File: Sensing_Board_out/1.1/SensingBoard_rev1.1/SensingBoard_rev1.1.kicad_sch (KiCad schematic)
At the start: 52 parts, among them J1 USB_C_Receptacle, J3 F32R-1A7H1-11024, J4 GRPB052VWQP-RC, J5 HMTSW-102-X-X-S-X, J6 HMTSW-102-X-X-S-X, J7 3221-10-0300-00, J7 HMTSW-102-X-X-S-X, J8 HMTSW-102-X-X-S-X, SW1 PTS815 SJM 250 SMTR LFS, U1 ESP32C3, U2 BNO055, U3 MIC5504-3.3YM5, U4 FT232RQ

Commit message: finished power board
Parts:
- removed J5, J6, J7, J8: HMTSW-102-X-X-S-X, HMTSW-102-X-X-S-X:SAMTEC_HMTSW-102-X-X-S-X, symbol HMTSW-102-X-X-S-X:HMTSW-102-X-X-S-X
- added C10 (x4): 1uF, Capacitor_SMD:C_0201_0603Metric, symbol Device:C
- added C14 (x2): 18pF, Capacitor_SMD:C_0201_0603Metric, symbol Device:C
- added C17 (x2): 1.6pF, Capacitor_SMD:C_0402_1005Metric, symbol Device:C
- added C17: 100nF, Capacitor_SMD:C_0402_1005Metric, symbol Device:C
- added C9: 2.2uF, Capacitor_SMD:C_0402_1005Metric, symbol Device:C
- added C9 (x4): 10uF, Capacitor_SMD:C_0603_1608Metric, symbol Device:C
- added FB1: 120R-3A, Capacitor_SMD:C_0805_2012Metric, symbol Device:FerriteBead
- added J5, J6, J7, J9: RS1-02-G, CONN_RS1-02-G_ADM, symbol RS1-02-G:RS1-02-G
- added L1, L2: 2nH, Inductor_SMD:L_01005_0402Metric, symbol Device:L
- added R14 (x3), R15: 10k, Resistor_SMD:R_0201_0603Metric, symbol Device:R_US
- added SW2: PTS815 SJM 250 SMTR LFS, SW4_PTS815 SJM 250 SMTR LFS_CNK, symbol PTS815:PTS815_SJM_250_SMTR_LFS
- added U5: MIC5504-1.8YM5, Package_TO_SOT_SMD:SOT-23-5, symbol Regulator_Linear:MIC5504-1.8YM5
- added U6: MCP1700x-280xxTT, Package_TO_SOT_SMD:SOT-23, symbol Regulator_Linear:MCP1700x-280xxTT
- added Y1: ABM8G-40.000MHZ-18-D2Y-T, CRYSTAL_ABM8G_ABR, symbol ABM8G_40_000MHZ_18_D2Y_T:ABM8G-40.000MHZ-18-D2Y-T
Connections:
- net +3.3V: now also U1.17 (VDD3P3_CPU), U1.31 (VDDA), U1.32 (VDDA), L2.1, R14.1, R15.1; no longer U1.2 (VDD3P3), U1.3 (VDD3P3)
- net D9: now also SW2.1
- net DRV_FAULT: now also J7.1
- net DRV_SLEEP: now also J7.2
- net GND: now also ANT1.GND1, ANT1.GND2, C16.1, C17.2, J3.2, C10.2, C10.2, C10.2, C10.2, C14.2, C14.2, C17.2, C17.2, C17.2, C9.2, C9.2, C9.2, C9.2, C9.2, J9.1, SW2.4, U5.2 (GND), U6.1 (GND), Y1.2 (GND), Y1.4 (GND)
- net MOTOR1_AIN1: now also J5.2
- net MOTOR1_AIN2: now also J5.1
- net MOTOR2_BIN1: now also J6.2
- net MOTOR2_BIN2: now also J6.1
- net VDC: now also C10.1, C10.1, C9.1, C9.1, J9.2, U5.1 (VIN), U5.3 (EN), U6.3 (VI)
- net at ANT1.SIG: now also C17.1, L1.2
- net CHIP_EN: now reaches SW1.1
- net CHIP_EN: now also U1.7 (CHIP_EN)
- net at U1.1 (LNA_IN): now also C17.1, L1.1
- net VDD3P3_RTC: now reaches U1.11 (VDD3P3_RTC)
- net VDD_SPI: now reaches U1.18 (VDD_SPI)
- net SPIHD: now reaches U1.19 (SPIHD)
- net SPIWP: now reaches U1.20 (SPIWP)
- net SPICS0: now reaches U1.21 (SPICS0)
- net SPICLK: now reaches U1.22 (SPICLK)
- net SPID: now reaches U1.23 (SPID)
- net SPIQ: now reaches U1.24 (SPIQ)
- net at U1.29 (XTAL_N): now also C14.1, Y1.1
- net at U1.30 (XTAL_P): now also C14.1, Y1.3
- net IO40/CAM_SDA: now reaches J3.3
- net IO40/CAM_SDA: now also R14.2
- net at J3.4: now also FB1.2
- net IO39/CAM_SCL: now reaches J3.5
- net IO39/CAM_SCL: now also R14.2
- net CAM_RESET: now reaches J3.6
- net CAM_RESET: now also R14.2
- new net: C17.1, L2.2, U1.2 (VDD3P3), U1.3 (VDD3P3)
- new net: R15.2, SW2.2
- new net +1V8: C10.1, C9.1, U5.5 (VOUT)
- new net +2V8: C10.1, C9.1, C9.1, FB1.1, R14.1, R14.1, U6.2 (VO)
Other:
- note added: "1v8 LDO"
- note added: "2v8 LDO"
- note added: "B2B HEADERS (female)"
- note added: "BOOT"
- note added: "RESET"
- note removed: "B2B HEADERS"
- moved on the sheet: ANT1, C10, C14, C15, C16, C17, D5, D6, J3, J4, R11, R12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

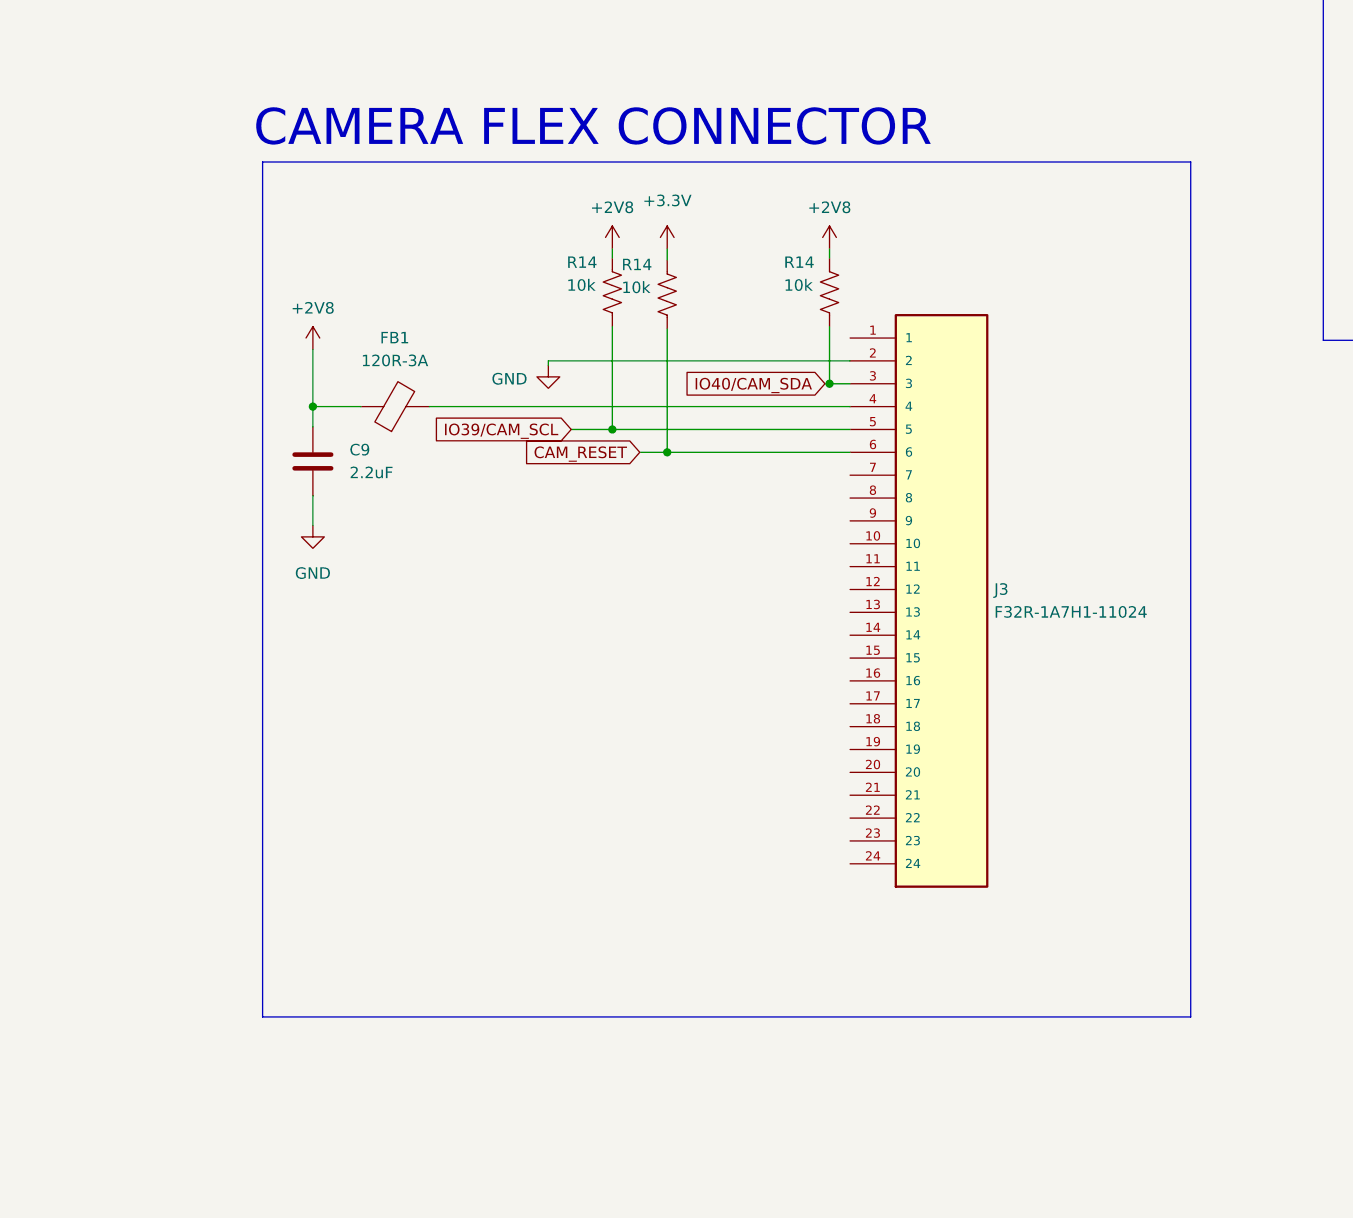
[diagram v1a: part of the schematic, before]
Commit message: fixing POE board symbols + circuit
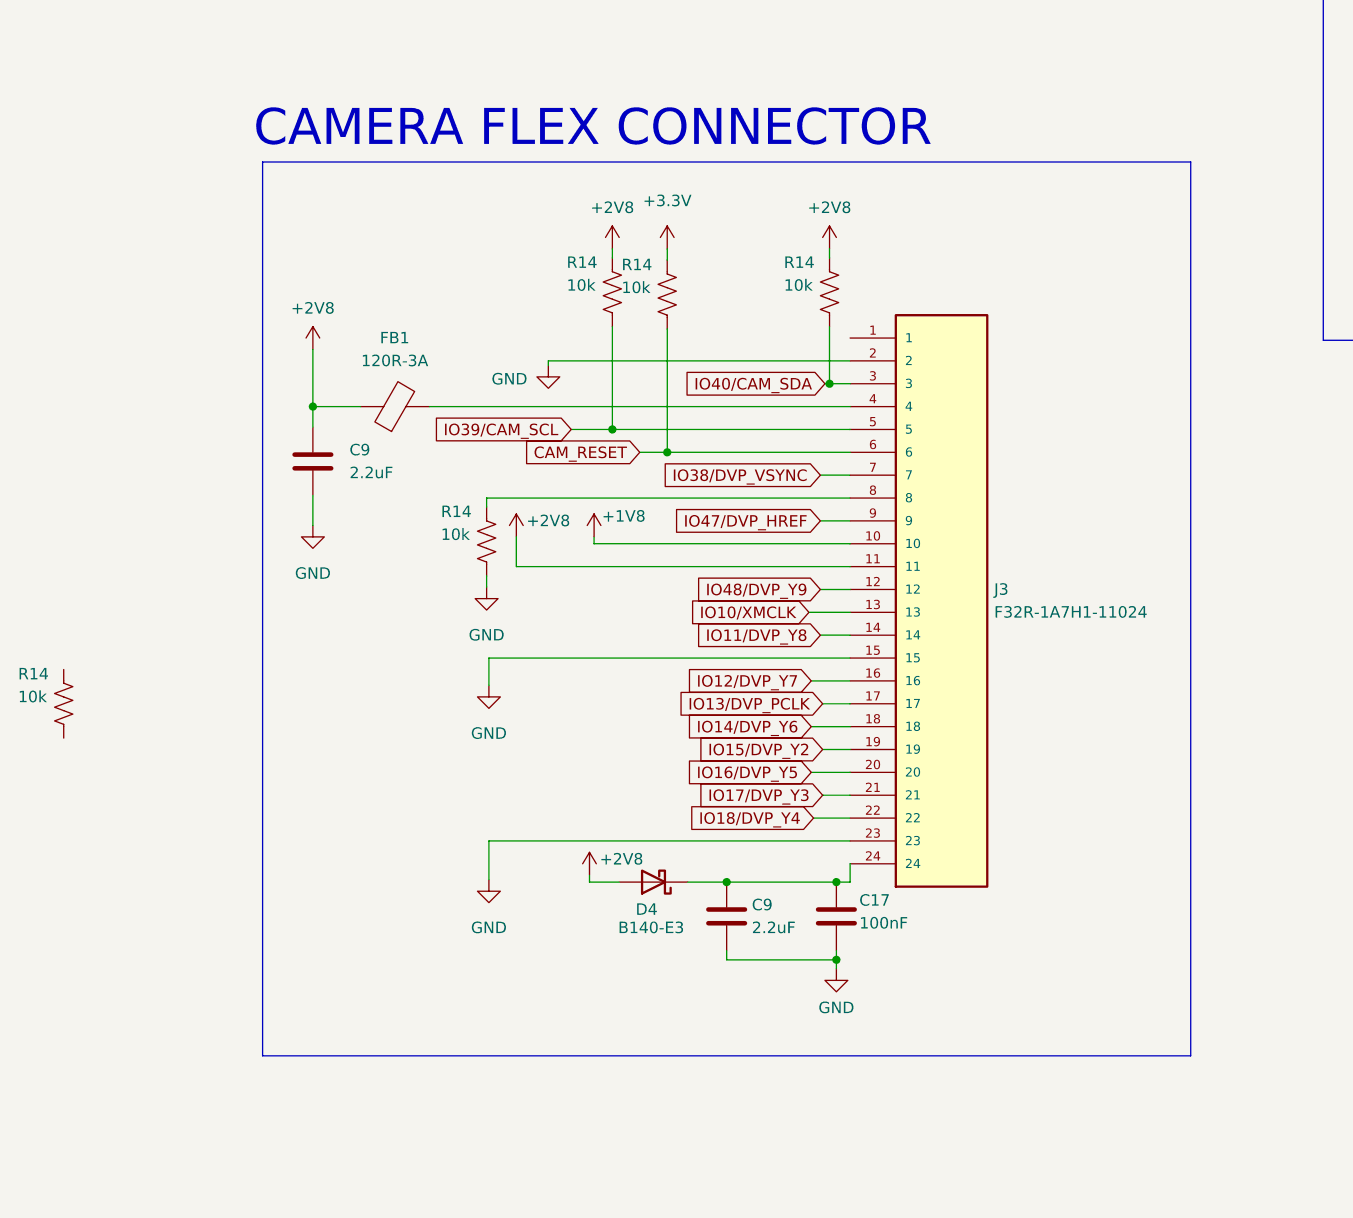
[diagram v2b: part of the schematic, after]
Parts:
- added C17: 100nF, Capacitor_SMD:C_0402_1005Metric, symbol Device:C
- added C9: 2.2uF, Capacitor_SMD:C_0402_1005Metric, symbol Device:C
- added D4: B140-E3, Diode_SMD:D_SMA, symbol Diode:B140-E3
- added R14 (x2): 10k, Resistor_SMD:R_0201_0603Metric, symbol Device:R_US
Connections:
- net +1V8: now also J3.10
- net +2V8: now also J3.11, D4.2 (A)
- net GND: now also J3.15, J3.23, C17.2, C9.2, R14.2
- net IO48/DVP_Y9: now reaches J3.12
- net IO10/XMCLK: now reaches J3.13
- net IO11/DVP_Y8: now reaches J3.14
- net IO12/DVP_Y7: now reaches J3.16
- net IO13/DVP_PCLK: now reaches J3.17
- net IO14/DVP_Y6: now reaches J3.18
- net IO15/DVP_Y2: now reaches J3.19
- net IO16/DVP_Y5: now reaches J3.20
- net IO17/DVP_Y3: now reaches J3.21
- net IO18/DVP_Y4: now reaches J3.22
- net at J3.24: now also C17.1, C9.1, D4.1 (K)
- net IO38/DVP_VSYNC: now reaches J3.7
- net at J3.8: now also R14.1
- net IO47/DVP_HREF: now reaches J3.9

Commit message: updates
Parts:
- removed R14: 10k, Resistor_SMD:R_0201_0603Metric, symbol Device:R_US
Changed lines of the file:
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@@
-    )
-  )
-  (symbol (lib_id "Device:R_US") (at 0 285.75 0) (unit 1)
-    (in_bom yes) (on_board yes) (dnp no)
-    (property "Reference" "R14" (at -5.08 282.448 0)
-      (effects (font (size 1.27 1.27)) (justify left))
-    )
-    (property "Value" "10k" (at -5.08 284.988 0)
-      (effects (font (size 1.27 1.27)) (justify left))
-    )
-    (property "Footprint" "Resistor_SMD:R_0201_0603Metric" (at 1.016 286.004 90)
-      (effects (font (size 1.27 1.27)) hide)
-    )
-    (property "Datasheet" "~" (at 0 285.75 0)
-      (effects (font (size 1.27 1.27)) hide)
-    )
-    (pin "1")
-    (pin "2")
-    (instances
-      (project "MachGen1B"
-        (path "/a8d93769-5183-4e19-8aae-3bec0e5cb94a"
-          (reference "R14") (unit 1)
-        )
-      )
-      (project "SensingBoard_rev1.1"
-        (path "/b61d80ec-963d-4516-bd15-8e7f6f5207da"
-          (reference "R26") (unit 1)
-        )
-      )
     )
   )

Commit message: updates
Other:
- note added: "Schematic Review: Swap with ESP32S3"
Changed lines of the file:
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@@
     (effects (font (size 4 4)) (justify left bottom))
+  )
+  (text "Schematic Review:\nSwap with ESP32S3" (at 607.314 143.256 0)
+    (effects (font (size 1.27 1.27)) (justify left bottom))
   )
   (text "HEADERS" (at 468.122 27.94 0)

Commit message: sense board
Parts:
- removed C14, C15: 22pF, Capacitor_SMD:C_0201_0603Metric, symbol Device:C
- removed C16: 10uF, Capacitor_SMD:C_0603_1608Metric, symbol Device:C
- removed C17: 100nF, Capacitor_SMD:C_0402_1005Metric, symbol Device:C
- removed C17: 1uF, Capacitor_SMD:C_0201_0603Metric, symbol Device:C
- removed J4: GRPB052VWQP-RC, GRPB052VWQP-RC:GRPB052VWQPRC, symbol GRPB052VWQP-RC:GRPB052VWQP-RC
- removed R14 (x3): 10k, Resistor_SMD:R_0201_0603Metric, symbol Device:R_US
- removed U1: ESP32C3, ESP32C3:QFN32_5X5MM, symbol ESP32C3:ESP32C3
- removed XTAL1: ABS07-32.768KHZ-7-T, XTAL_ABS07-32.768KHZ-7-T_ABR, symbol ABS07-32.768KHZ-7-T:ABS07-32.768KHZ-7-T
- added C17 (x7): 100nF, Capacitor_SMD:C_0402_1005Metric, symbol Device:C
- added C17: 10nF, Capacitor_SMD:C_0402_1005Metric, symbol Device:C
- added C17: 4.7uF, Capacitor_SMD:C_0402_1005Metric, symbol Device:C
- added C9 (x3): 2.2uF, Capacitor_SMD:C_0402_1005Metric, symbol Device:C
- added R11 (x2): 0k, Resistor_SMD:R_0201_0603Metric, symbol Device:R_US
- added R14: 10k, Resistor_SMD:R_0201_0603Metric, symbol Device:R_US
- added R14 (x2): 4.7k, Resistor_SMD:R_0201_0603Metric, symbol Device:R_US
- added R14: 499, Resistor_SMD:R_0201_0603Metric, symbol Device:R_US
- added U7: ESP32-S3, QFN56_7X7_EXP, symbol ESP32S3:ESP32-S3
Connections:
- net +2V8: now also R11.2
- net +3.3V: now also C17.1, C17.1, C17.1, C17.1, C17.1, C17.1, C17.1, C9.1, C9.1, C9.1, R11.2, R14.1, U7.20 (VDD3P3_RTC), U7.46 (VDD3P3_CPU), U7.55 (VDDA), U7.56 (VDDA)
- net CAM_RESET: now also C17.1, R14.2
- net CHIP_EN: now also U7.4 (CHIP_PU)
- net GND: now also C17.2, C17.2, C17.2, C17.2, C17.2, C17.2, C17.2, C17.2, C17.2, C9.2, C9.2, C9.2, U7.57 (GND)
- net IO10/XMCLK: now also U7.15 (GPIO10)
- net IO11/DVP_Y8: now also U7.16 (GPIO11)
- net IO12/DVP_Y7: now also U7.17 (GPIO12)
- net IO13/DVP_PCLK: now also U7.18 (GPIO13)
- net IO14/DVP_Y6: now also U7.19 (GPIO14)
- net IO15/DVP_Y2: now also U7.21 (XTAL_32K_P)
- net IO16/DVP_Y5: now also U7.22 (XTAL_32K_N)
- net IO17/DVP_Y3: now also U7.23 (GPIO17)
- net IO18/DVP_Y4: now also U7.24 (GPIO18)
- net IO38/DVP_VSYNC: now also U7.43 (GPIO38)
- net IO47/DVP_HREF: now also U7.37 (SPICLK_P)
- net IO48/DVP_Y9: now also U7.36 (SPICLK_N)
- net RX_D7: now also U7.50 (U0RXD)
- net SPICLK: now also U7.33 (SPICLK)
- net SPICS0: now also U7.32 (SPICS0)
- net SPID: now also U7.35 (SPID)
- net SPIHD: now also U7.30 (SPIHD)
- net SPIQ: now also U7.34 (SPIQ)
- net SPIWP: now also U7.31 (SPIWP)
- net TX_D6: now also R14.2
- net USB_DN: now also U7.25 (GPIO19)
- net USB_DP: now also U7.26 (GPIO20)
- net VDD_SPI: now also U7.29 (VDD_SPI)
- net at C14.1, Y1.1: now also U7.53 (XTAL_N)
- net at C14.1, Y1.3: now also U7.54 (XTAL_P)
- net at L2.2: now also C17.1, U7.2 (VDD3P3), U7.3 (VDD3P3)
- net at C17.1, L1.1: now also U7.1 (LNA_IN)
- net IO39/CAM_SCL renamed MTCK/IO39/CAM_SCL
- net MTCK/IO39/CAM_SCL: now also R14.2, U7.44 (MTCK)
- net IO40/CAM_SDA renamed MTDO/IO40/CAM_SDA
- net MTDO/IO40/CAM_SDA: now also R14.2, U7.45 (MTDO)
- new net: R11.1, R11.1, R14.1, R14.1
- new net: R14.1, U7.49 (U0TXD)
- new net D0/A0: U7.6 (GPIO1)
- new net D10/A10/MOSI: U7.14 (GPIO9)
- new net D1/A1: U7.7 (GPIO2)
- new net D2/A2: U7.8 (GPIO3)
- new net D3/A3: U7.9 (GPIO4)
- new net D4/I2C_SDA: U7.10 (GPIO5)
- new net D5/I2C_SCL: U7.11 (GPIO6)
- new net D8/A8/SCK: U7.12 (GPIO7)
- new net D9/A9/MISO: U7.13 (GPIO8)
- new net GPIO0: U7.5 (GPIO0)
- new net IO21/USER_LED: U7.27 (GPIO21)
- new net MTDI/IO41/PDM_DATA: U7.47 (MTDI)
- new net MTMS/IO42/PDM_CLK: U7.48 (MTMS)
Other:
- note removed: "HEADERS"
- note removed: "Schematic Review: Swap with ESP32S3"
- moved on the sheet: ANT1, C14, C17, J3, L1, Y1

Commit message: completed sense board
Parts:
- removed D5: LED, LED_SMD:LED_0603_1608Metric, symbol Device:LED
- removed R17: 100, Resistor_SMD:R_0201_0603Metric, symbol Device:R_US
- added C17: 100nF, Capacitor_SMD:C_0402_1005Metric, symbol Device:C
- added U8: GD25D05CT, Package_SO:SOP-8_3.9x4.9mm_P1.27mm, symbol Memory_Flash:GD25D05CT
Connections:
- net D9 is gone; now on net GPIO0: SW2.1
- net +3.3V: now also R16.2, C17.1, U8.8 (VCC)
- net D0/A0: now also R12.2
- net D1/A1: now also R12.2
- net D2/A2: now also R12.2
- net D3/A3: now also R12.2
- net GND: now also C17.2, U8.4 (VSS)
- net IO21/USER_LED: now also D6.1 (K)
- net SPICLK: now also U8.6 (SCLK)
- net SPICS0: now also U8.1 (~{CS})
- net SPID: now also U8.5 (SI/IO0)
- net SPIQ: now also U8.2 (O1/SO)
- net SPIWP: now also U8.3 (~{WP})
- net GPIO34: now reaches R11.2
- net GPIO34: now also U7.39 (GPIO34)
- net at R16.1: now also D6.2 (A)
- net GPIO33: now reaches R11.2
- net GPIO33: now also U7.38 (GPIO33)
- net GPIO37: now reaches R11.2
- net GPIO37: now also U7.42 (GPIO37)
- net GPIO35: now reaches R11.2
- net GPIO35: now also U7.40 (GPIO35)
- net GPIO36: now reaches R11.2
- net GPIO36: now also U7.41 (GPIO36)

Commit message: power board layout
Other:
- moved on the sheet: C17
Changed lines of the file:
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@@
     (stroke (width 0) (type default))
   )
-  (wire (pts (xy 541.274 243.586) (xy 541.274 241.3))
+  (wire (pts (xy 541.274 243.586) (xy 541.274 241.808))
     (stroke (width 0) (type default))
   )
@@
     (stroke (width 0) (type default))
   )
-  (wire (pts (xy 541.274 233.68) (xy 541.274 232.41))
+  (wire (pts (xy 541.274 234.188) (xy 541.274 232.41))
     (stroke (width 0) (type default))
   )
@@
     )
   )
-  (symbol (lib_id "Device:C") (at 541.274 237.49 0) (unit 1)
+  (symbol (lib_id "Device:C") (at 541.274 237.998 0) (unit 1)
     (in_bom yes) (on_board yes) (dnp no)
-    (property "Reference" "C17" (at 543.814 235.712 0)
+    (property "Reference" "C17" (at 543.814 236.22 0)
       (effects (font (size 1.27 1.27)) (justify left))
     )
-    (property "Value" "100nF" (at 543.814 238.252 0)
+    (property "Value" "100nF" (at 543.814 238.76 0)
       (effects (font (size 1.27 1.27)) (justify left))
     )
-    (property "Footprint" "Capacitor_SMD:C_0402_1005Metric" (at 542.2392 241.3 0)
+    (property "Footprint" "Capacitor_SMD:C_0402_1005Metric" (at 542.2392 241.808 0)
       (effects (font (size 1.27 1.27)) hide)
     )
-    (property "Datasheet" "~" (at 541.274 237.49 0)
+    (property "Datasheet" "~" (at 541.274 237.998 0)
       (effects (font (size 1.27 1.27)) hide)
     )
